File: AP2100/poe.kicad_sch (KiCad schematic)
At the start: 135 parts, among them IC2 PM8805TR, IC3 PM8804TR, J1 0826-1X1T-GH-F, J2 Barrel_Jack, Q1 BSC190N15NS3GATMA1, Q4 FDMC86259P, Q5 FOD817AS, U6 TS2431-AILT

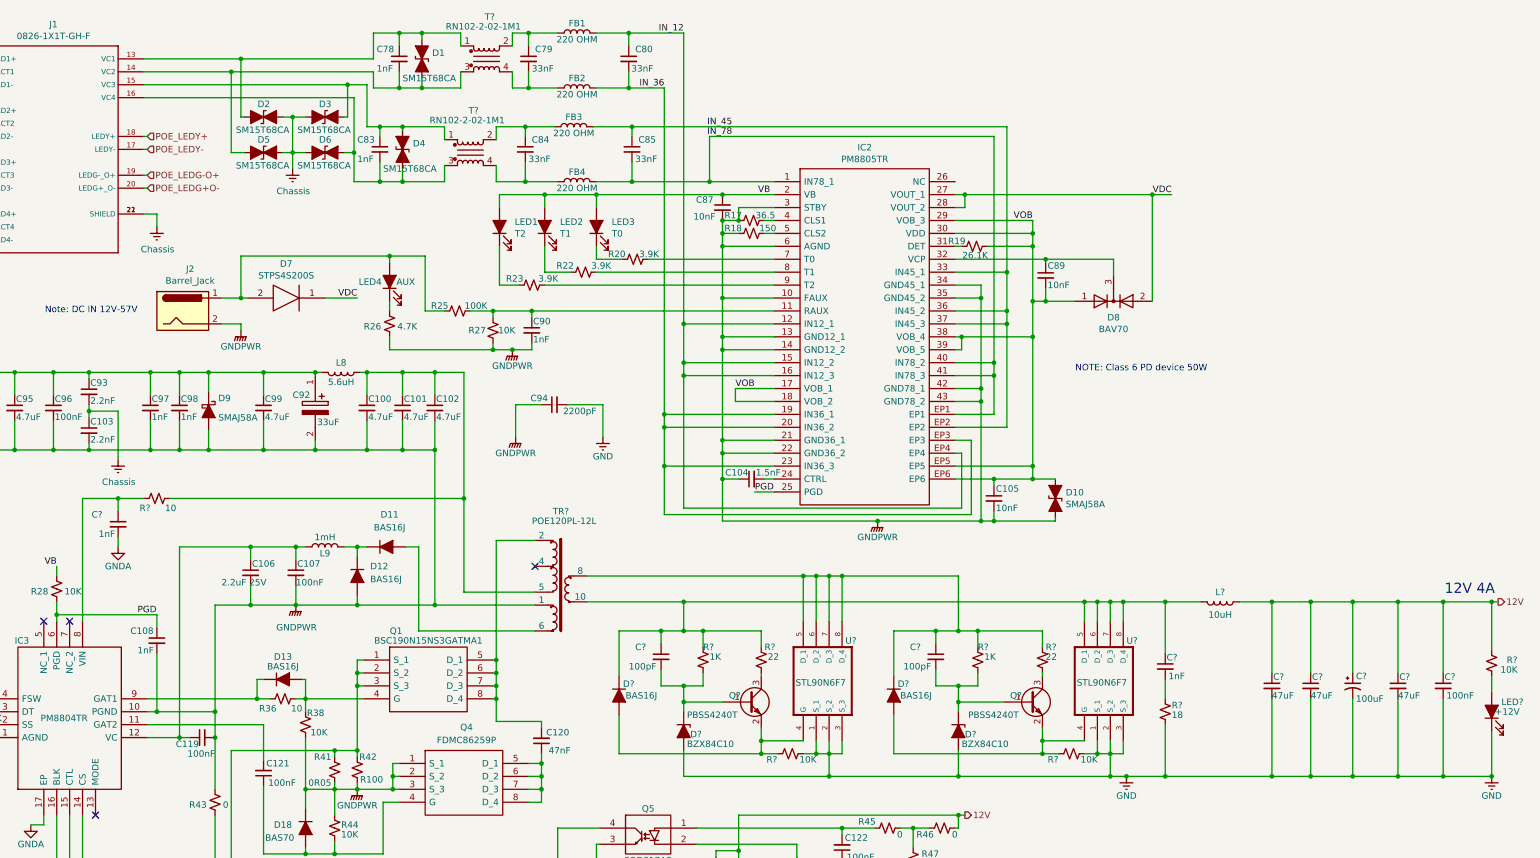
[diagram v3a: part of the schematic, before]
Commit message: Finish Power PoE section layout
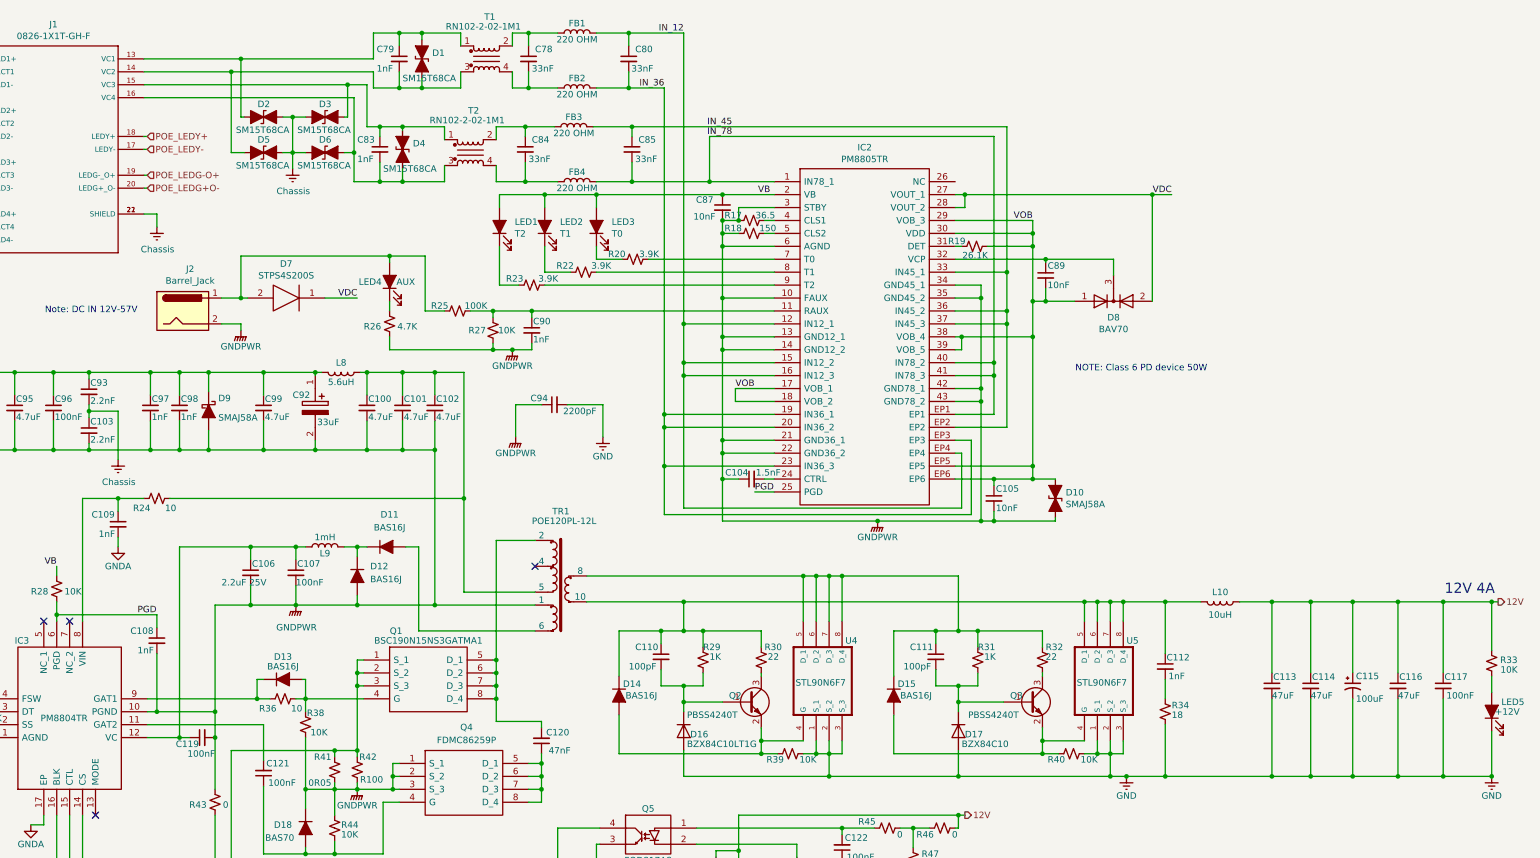
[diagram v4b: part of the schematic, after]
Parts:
- D16: renamed from D?; value BZX84C10 -> BZX84C10LT1G; symbol Device:D_Zener_ALT -> Diode:BAS19; PartsBoxID BZX84C10 -> BZX84C10LT1G
- D17: renamed from D?; symbol Device:D_Zener_ALT -> Diode:BAS19
- Q1: footprint LIB_BSC190N15NS3GATMA1:PG-TDSON-8_1 -> Package_TO_SOT_SMD:TDSON-8-1
- gave numbers to parts that had none: 29
- renumbered C79 to C78, C78 to C79
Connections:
- net GND: now also D16.1 (A), D17.1 (A); no longer C103.1, C81.1, C82.1, C86.1, C88.1, C93.2, D16.2 (A), D17.2 (A), D2.1 (A1), D3.2 (A2), D5.1 (A1), D6.2 (A2), J1.21 (SHIELD), J1.22 (SHIELD), R21.2
- net at C111.2, Q3.1 (B), R31.2: now also D17.3 (K); no longer D17.1 (K)
- net at C110.2, Q2.1 (B), R29.2: now also D16.3 (K); no longer D16.1 (K)
- new net Earth: C103.1, C81.1, C82.1, C86.1, C88.1, C93.2, D2.1 (A1), D3.2 (A2), D5.1 (A1), D6.2 (A2), J1.21 (SHIELD), J1.22 (SHIELD), R21.2

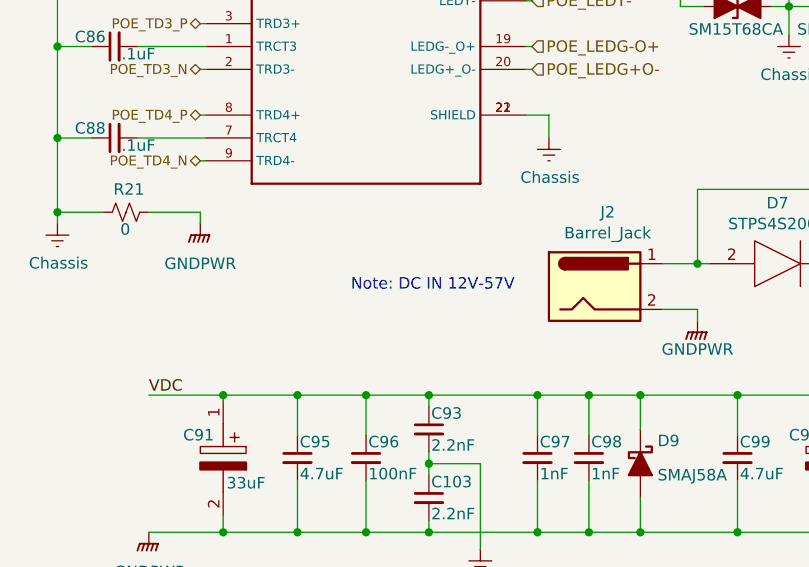
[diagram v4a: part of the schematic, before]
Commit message: Fixup broken BSC100 footprint with missing pins Add mPCIE footprint with retainer holes Review / complete PartsBox info
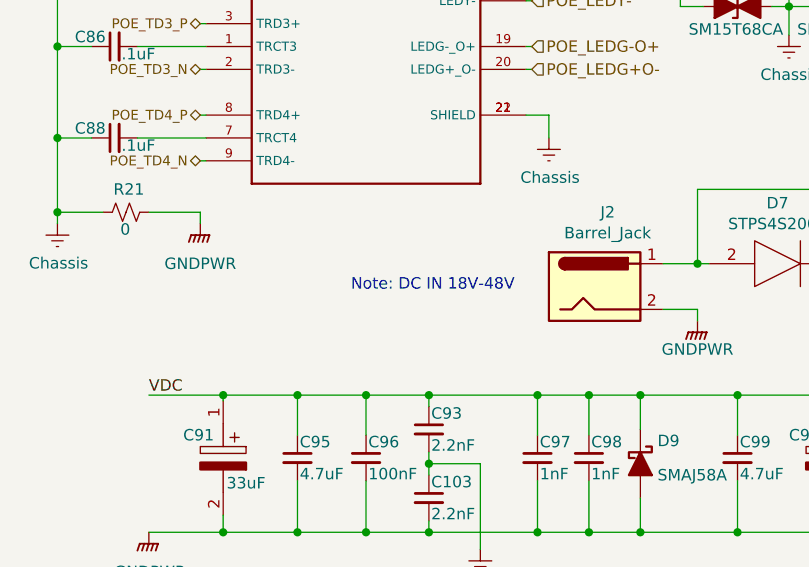
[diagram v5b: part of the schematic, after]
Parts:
- C109: PartsBoxID 0805-1nF-X7R-100V -> 0805-1nF-X7R-250V
- Q1: footprint Package_TO_SOT_SMD:TDSON-8-1 -> Scott:TRANS_BSC100N06LS3GATMA1
- R17: PartsBoxID 0805-36.5R-1% -> 0805-36R5-1%
- T1, T2: PartsBoxID (none) -> RN102-2-02-1M1
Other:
- note added: "Note: DC IN 18V-48V"
- note removed: "Note: DC IN 12V-57V"
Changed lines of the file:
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@@
   (junction (at 365.125 149.225) (diameter 0.9144) (color 0 0 0 0))
   (junction (at 365.125 183.515) (diameter 0.9144) (color 0 0 0 0))
-  (no_connect (at 90.805 191.135))
   (no_connect (at 85.725 153.035))
   (no_connect (at 80.645 153.035))
+  (no_connect (at 90.805 191.135))
   (no_connect (at 177.165 142.24))
   (wire (pts (xy 48.26 45.085) (xy 52.07 45.085))
@@
     (stroke (width 0) (type solid) (color 0 0 0 0))
   )
-  (text "Note: DC IN 12V-57V" (at 99.06 92.71 180)
+  (text "Note: DC IN 18V-48V" (at 99.06 92.71 180)
     (effects (font (size 1.27 1.27)) (justify right bottom))
   )
@@
       (effects (font (size 1.27 1.27)) hide)
     )
-    (property "PartsBoxID" "0805-36.5R-1%" (id 4) (at 219.71 74.295 0)
+    (property "PartsBoxID" "0805-36R5-1%" (id 4) (at 219.71 74.295 0)
       (effects (font (size 1.27 1.27)) hide)
     )
@@
       (effects (font (size 1.27 1.27)) hide)
     )
-    (property "PartsBoxID" "0805-1nF-X7R-100V" (id 4) (at 95.25 133.985 0)
+    (property "PartsBoxID" "0805-1nF-X7R-250V" (id 4) (at 95.25 133.985 0)
       (effects (font (size 1.27 1.27)) hide)
     )
@@
       (effects (font (size 1.27 1.27)) hide)
     )
+    (property "PartsBoxID" "RN102-2-02-1M1" (id 4) (at 164.465 60.96 0)
+      (effects (font (size 1.27 1.27)) hide)
+    )
   )
   (symbol (lib_id "Filter:Choke_Schaffner_RN102-2-02-1M1") (at 167.64 42.545 0) (unit 1)
@@
       (effects (font (size 1.27 1.27)) hide)
     )
+    (property "PartsBoxID" "RN102-2-02-1M1" (id 4) (at 167.64 42.545 0)
+      (effects (font (size 1.27 1.27)) hide)
+    )
   )
   (symbol (lib_id "dk_PMIC-Voltage-Reference:TL431AIDBZR") (at 228.6 215.9 0) (unit 1)
@@
     (property "Reference" "Q1" (id 0) (at 149.86 154.94 0))
     (property "Value" "BSC190N15NS3GATMA1" (id 1) (at 156.21 156.845 0))
-    (property "Footprint" "Package_TO_SOT_SMD:TDSON-8-1" (id 2) (at 165.1 158.115 0)
+    (property "Footprint" "Scott:TRANS_BSC100N06LS3GATMA1" (id 2) (at 165.1 158.115 0)
       (effects (font (size 1.27 1.27)) (justify left) hide)
     )

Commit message: Revise BOM
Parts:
- added R311: 1K, Resistor_SMD:R_0603_1608Metric, symbol Device:R_Small_US
- C106, C127: footprint Capacitor_SMD:C_0603_1608Metric -> Capacitor_SMD:C_0805_2012Metric; PartsBoxID 0603-2.2uF-X7R-25V -> 0805-2.2uF-X7R-25V
- C91, C92: PartsBoxID EEEFK2A330P -> EEE-FK2A330P
- C94: value 2200pF -> 2.2nF; PartsBoxID 1812-2200pF-X7R-2KV -> 1812-2.2nF-X7R-2KV
- L8: MPN (none) -> XAL5050-562MEB; PartsBoxID XAL50-56-R -> XAL50-5.6-R
- Q2, Q3: PartsBoxID PBSS4240T -> PBSS4240T,215
- R35: value 91K -> 88.7K; PartsBoxID 0603-91K-1% -> 0603-88.7K-1%
- TR1: PartsBoxID POE120PL-12L -> POE120PL-12L_
- U6: PartsBoxID TS2431-AILT -> TS2431AILT
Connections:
- net GNDA: now also R311.1; no longer R35.1
- new net: R311.2, R35.1
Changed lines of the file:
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@@
-(kicad_sch (version 20200828) (generator eeschema)
-  (page 3 12)
+(kicad_sch (version 20201015) (generator eeschema)
+  (page 1 12)
   (paper "USLedger")
   (title_block
@@
   (junction (at 365.125 149.225) (diameter 0.9144) (color 0 0 0 0))
   (junction (at 365.125 183.515) (diameter 0.9144) (color 0 0 0 0))
-  (no_connect (at 85.725 153.035))
-  (no_connect (at 80.645 153.035))
   (no_connect (at 90.805 191.135))
+  (no_connect (at 80.645 153.035))
   (no_connect (at 177.165 142.24))
+  (no_connect (at 85.725 153.035))
   (wire (pts (xy 48.26 45.085) (xy 52.07 45.085))
     (stroke (width 0) (type solid) (color 0 0 0 0))
@@
     (stroke (width 0) (type solid) (color 0 0 0 0))
   )
-  (wire (pts (xy 53.34 168.275) (xy 62.23 168.275))
+  (wire (pts (xy 53.34 168.275) (xy 55.245 168.275))
     (stroke (width 0) (type solid) (color 0 0 0 0))
   )
@@
     (stroke (width 0) (type solid) (color 0 0 0 0))
   )
+  (wire (pts (xy 60.325 168.275) (xy 62.23 168.275))
+    (stroke (width 0) (type solid) (color 0 0 0 0))
+  )
   (wire (pts (xy 62.23 173.355) (xy 70.485 173.355))
     (stroke (width 0) (type solid) (color 0 0 0 0))
@@
       (effects (font (size 1.27 1.27)) (justify left) hide)
     )
-    (property "PartsBoxID" "XAL50-56-R" (id 4) (at 139.065 104.14 0)
+    (property "PartsBoxID" "XAL50-5.6-R" (id 4) (at 139.065 104.14 0)
       (effects (font (size 1.27 1.27)) hide)
     )
@@
       (effects (font (size 1.27 1.27)) (justify left) hide)
     )
+    (property "MPN" "XAL5050-562MEB \n" (id 4) (at 139.065 104.14 0)
+      (effects (font (size 1.27 1.27)) hide)
+    )
   )
   (symbol (lib_id "Device:L") (at 184.785 55.88 90) (unit 1)
@@
     )
   )
+  (symbol (lib_id "Device:R_Small_US") (at 57.785 168.275 90) (unit 1)
+    (in_bom yes) (on_board yes)
+    (property "Reference" "R311" (id 0) (at 56.515 167.005 90)
+      (effects (font (size 1.27 1.27)) (justify left))
+    )
+    (property "Value" "1K" (id 1) (at 62.23 167.005 90)
+      (effects (font (size 1.27 1.27)) (justify left))
+    )
+    (property "Footprint" "Resistor_SMD:R_0603_1608Metric" (id 2) (at 57.785 168.275 0)
+      (effects (font (size 1.27 1.27)) hide)
+    )
+    (property "Datasheet" "~" (id 3) (at 57.785 168.275 0)
+      (effects (font (size 1.27 1.27)) hide)
+    )
+    (property "PartsBoxID" "0603-1K-1%" (id 4) (at 57.785 168.275 0)
+      (effects (font (size 1.27 1.27)) hide)
+    )
+    (property "MPN" "-" (id 5) (at 132.715 198.755 0)
+      (effects (font (size 1.27 1.27)) hide)
+    )
+    (property "SPR" "-" (id 6) (at 132.715 198.755 0)
+      (effects (font (size 1.27 1.27)) hide)
+    )
+    (property "SPN" "-" (id 7) (at 132.715 198.755 0)
+      (effects (font (size 1.27 1.27)) hide)
+    )
+    (property "SPURL" "-" (id 8) (at 132.715 198.755 0)
+      (effects (font (size 1.27 1.27)) hide)
+    )
+  )
   (symbol (lib_id "Device:R_Small_US") (at 64.77 168.275 90) (unit 1)
     (in_bom yes) (on_board yes)
@@
       (effects (font (size 1.27 1.27)) (justify left))
     )
-    (property "Value" "91K" (id 1) (at 70.485 169.545 90)
+    (property "Value" "88.7K" (id 1) (at 72.39 169.545 90)
       (effects (font (size 1.27 1.27)) (justify left))
     )
@@
       (effects (font (size 1.27 1.27)) hide)
     )
-    (property "PartsBoxID" "0603-91K-1%" (id 4) (at 64.77 168.275 0)
+    (property "PartsBoxID" "0603-88.7K-1%" (id 4) (at 64.77 168.275 0)
       (effects (font (size 1.27 1.27)) hide)
     )
@@
       (effects (font (size 1.27 1.27)) (justify left))
     )
-    (property "Footprint" "Capacitor_SMD:C_0603_1608Metric" (id 2) (at 121.285 143.51 0)
+    (property "Footprint" "Capacitor_SMD:C_0805_2012Metric" (id 2) (at 121.285 143.51 0)
       (effects (font (size 1.27 1.27)) hide)
     )
@@
       (effects (font (size 1.27 1.27)) hide)
     )
-    (property "PartsBoxID" "0603-2.2uF-X7R-25V" (id 4) (at 121.285 143.51 0)
+    (property "PartsBoxID" "0805-2.2uF-X7R-25V" (id 4) (at 121.285 143.51 0)
       (effects (font (size 1.27 1.27)) hide)
     )
@@
       (effects (font (size 1.27 1.27)) (justify left))
     )
-    (property "Value" "2200pF" (id 1) (at 189.23 111.76 90)
+    (property "Value" "2.2nF" (id 1) (at 189.23 111.76 90)
       (effects (font (size 1.27 1.27)) (justify left))
     )
@@
       (effects (font (size 1.27 1.27)) hide)
     )
-    (property "PartsBoxID" "1812-2200pF-X7R-2KV" (id 4) (at 180.975 110.49 0)
+    (property "PartsBoxID" "1812-2.2nF-X7R-2KV" (id 4) (at 180.975 110.49 0)
       (effects (font (size 1.27 1.27)) hide)
     )
@@
       (effects (font (size 1.27 1.27)) (justify left))
     )
-    (property "Footprint" "Capacitor_SMD:C_0603_1608Metric" (id 2) (at 212.725 213.995 0)
+    (property "Footprint" "Capacitor_SMD:C_0805_2012Metric" (id 2) (at 212.725 213.995 0)
       (effects (font (size 1.27 1.27)) hide)
     )
@@
       (effects (font (size 1.27 1.27)) hide)
     )
-    (property "PartsBoxID" "0603-2.2uF-X7R-25V" (id 4) (at 212.725 213.995 0)
+    (property "PartsBoxID" "0805-2.2uF-X7R-25V" (id 4) (at 212.725 213.995 0)
       (effects (font (size 1.27 1.27)) hide)
     )
@@
       (effects (font (size 1.27 1.27)) (justify left) hide)
     )
-    (property "PartsBoxID" "EEEFK2A330P" (id 4) (at 66.675 104.775 0)
+    (property "PartsBoxID" "EEE-FK2A330P" (id 4) (at 66.675 104.775 0)
       (effects (font (size 1.27 1.27)) hide)
     )
@@
       (effects (font (size 1.27 1.27)) (justify left) hide)
     )
-    (property "PartsBoxID" "EEEFK2A330P" (id 4) (at 133.985 104.775 0)
+    (property "PartsBoxID" "EEE-FK2A330P" (id 4) (at 133.985 104.775 0)
       (effects (font (size 1.27 1.27)) hide)
     )
@@
       (effects (font (size 1.524 1.524)) (justify left) hide)
     )
-    (property "PartsBoxID" "TS2431-AILT" (id 4) (at 228.6 215.9 0)
+    (property "PartsBoxID" "TS2431AILT" (id 4) (at 228.6 215.9 0)
       (effects (font (size 1.27 1.27)) hide)
     )
@@
       (effects (font (size 1.27 1.27)) hide)
     )
-    (property "PartsBoxID" "PBSS4240T" (id 4) (at 219.075 168.91 0)
+    (property "PartsBoxID" "PBSS4240T,215" (id 4) (at 219.075 168.91 0)
       (effects (font (size 1.27 1.27)) hide)
     )
@@
       (effects (font (size 1.27 1.27)) hide)
     )
-    (property "PartsBoxID" "PBSS4240T" (id 4) (at 274.32 168.91 0)
+    (property "PartsBoxID" "PBSS4240T,215" (id 4) (at 274.32 168.91 0)
       (effects (font (size 1.27 1.27)) hide)
     )
@@
       (effects (font (size 1.27 1.27)) hide)
     )
-    (property "PartsBoxID" "POE120PL-12L" (id 4) (at 182.245 144.78 0)
+    (property "PartsBoxID" "POE120PL-12L_" (id 4) (at 182.245 144.78 0)
       (effects (font (size 1.27 1.27)) hide)
     )
